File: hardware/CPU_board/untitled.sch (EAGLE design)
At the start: 71 parts, among them IC1 MAX232ECWE, IC2 MAX232ECWE, IC3 AM29F040J, IC4 74HCT138D, IC5 LM2596S, IC6 74245SSOP, IC7 74245SSOP, IC8 74245SSOP, J2 POWER_JACKSLT, U1 AS6C4008-55SIN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

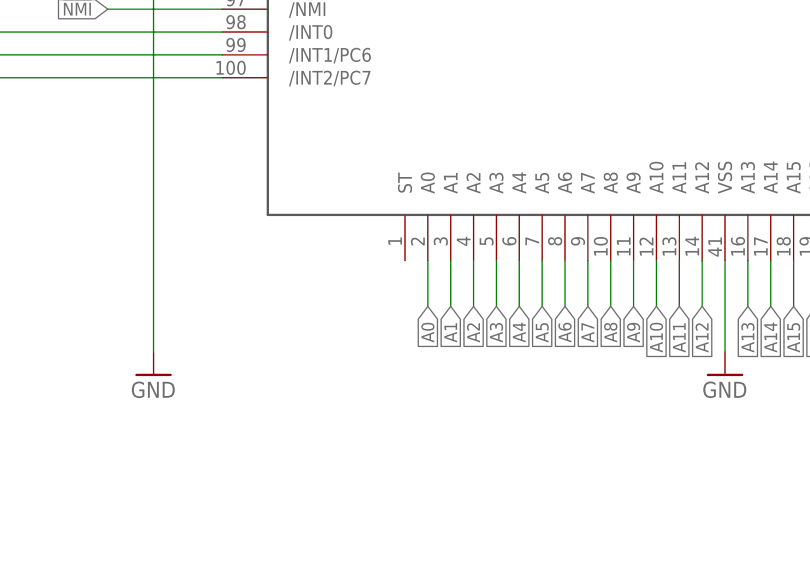
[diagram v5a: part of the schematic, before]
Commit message: ST signal connected (work in progress)
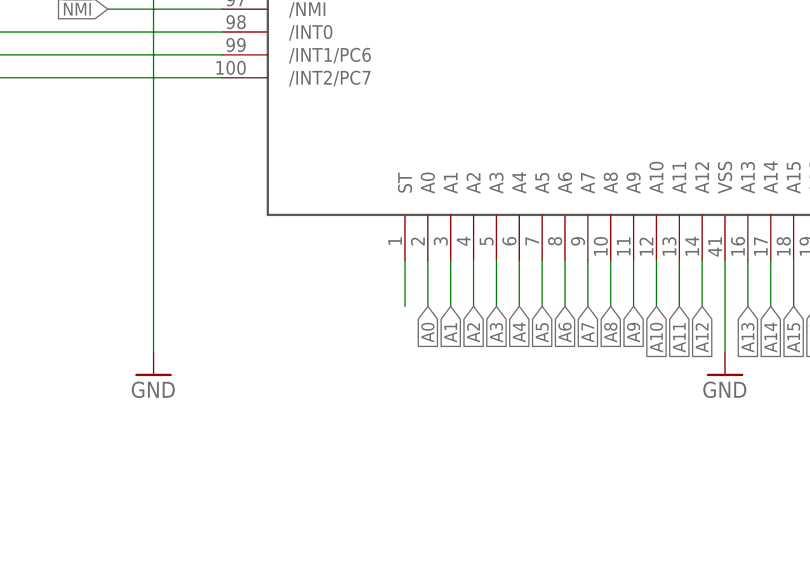
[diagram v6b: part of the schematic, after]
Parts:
- R10: device rcl:R-EU_R0603 -> rcl:R-EU_M1206
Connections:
- new net ST: U$1.ST
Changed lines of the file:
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@@
 <part name="JP5" library="pinhead" deviceset="PINHD-1X2" device=""/>
 <part name="GND16" library="supply1" deviceset="GND" device=""/>
-<part name="R10" library="rcl" deviceset="R-EU_" device="R0603"/>
+<part name="R10" library="rcl" deviceset="R-EU_" device="M1206"/>
 <part name="JP6" library="pinhead" deviceset="PINHD-1X2" device=""/>
 <part name="C21" library="rcl" deviceset="CPOL-EU" device="153CLV-0810" value="220uF"/>
@@
 </segment>
 </net>
+<net name="ST" class="0">
+<segment>
+<pinref part="U$1" gate="G$1" pin="ST"/>
+<wire x1="55.88" y1="35.56" x2="55.88" y2="30.48" width="0.1524" layer="91"/>
+</segment>
+</net>

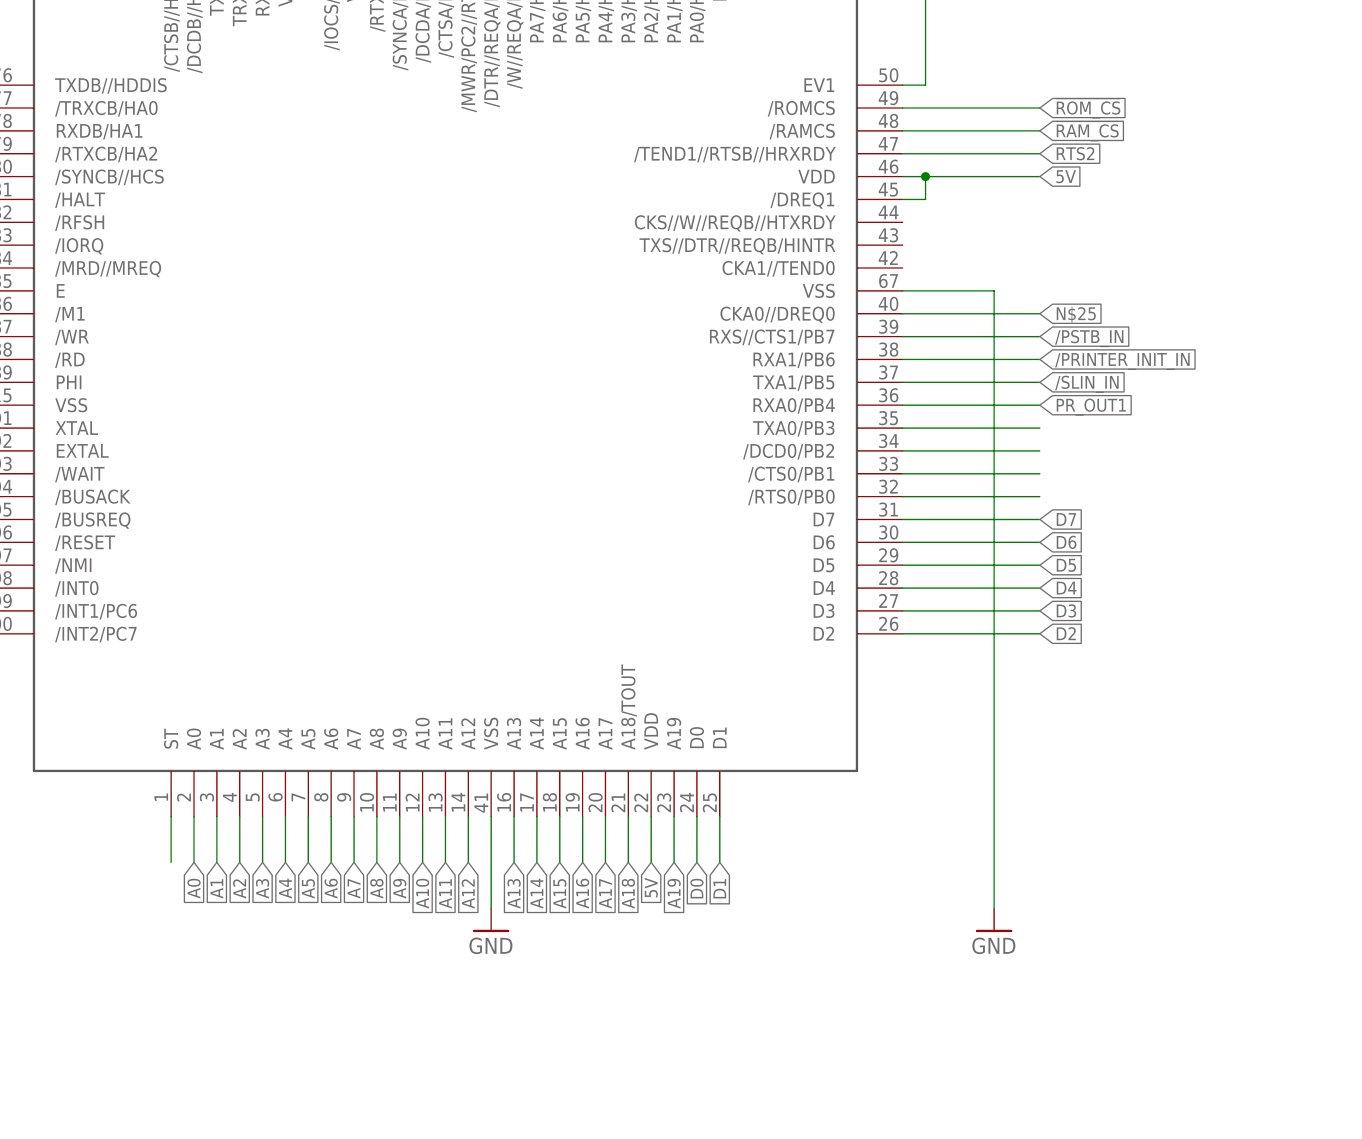
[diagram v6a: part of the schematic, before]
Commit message: Pull-up on ST and DREQ lines added
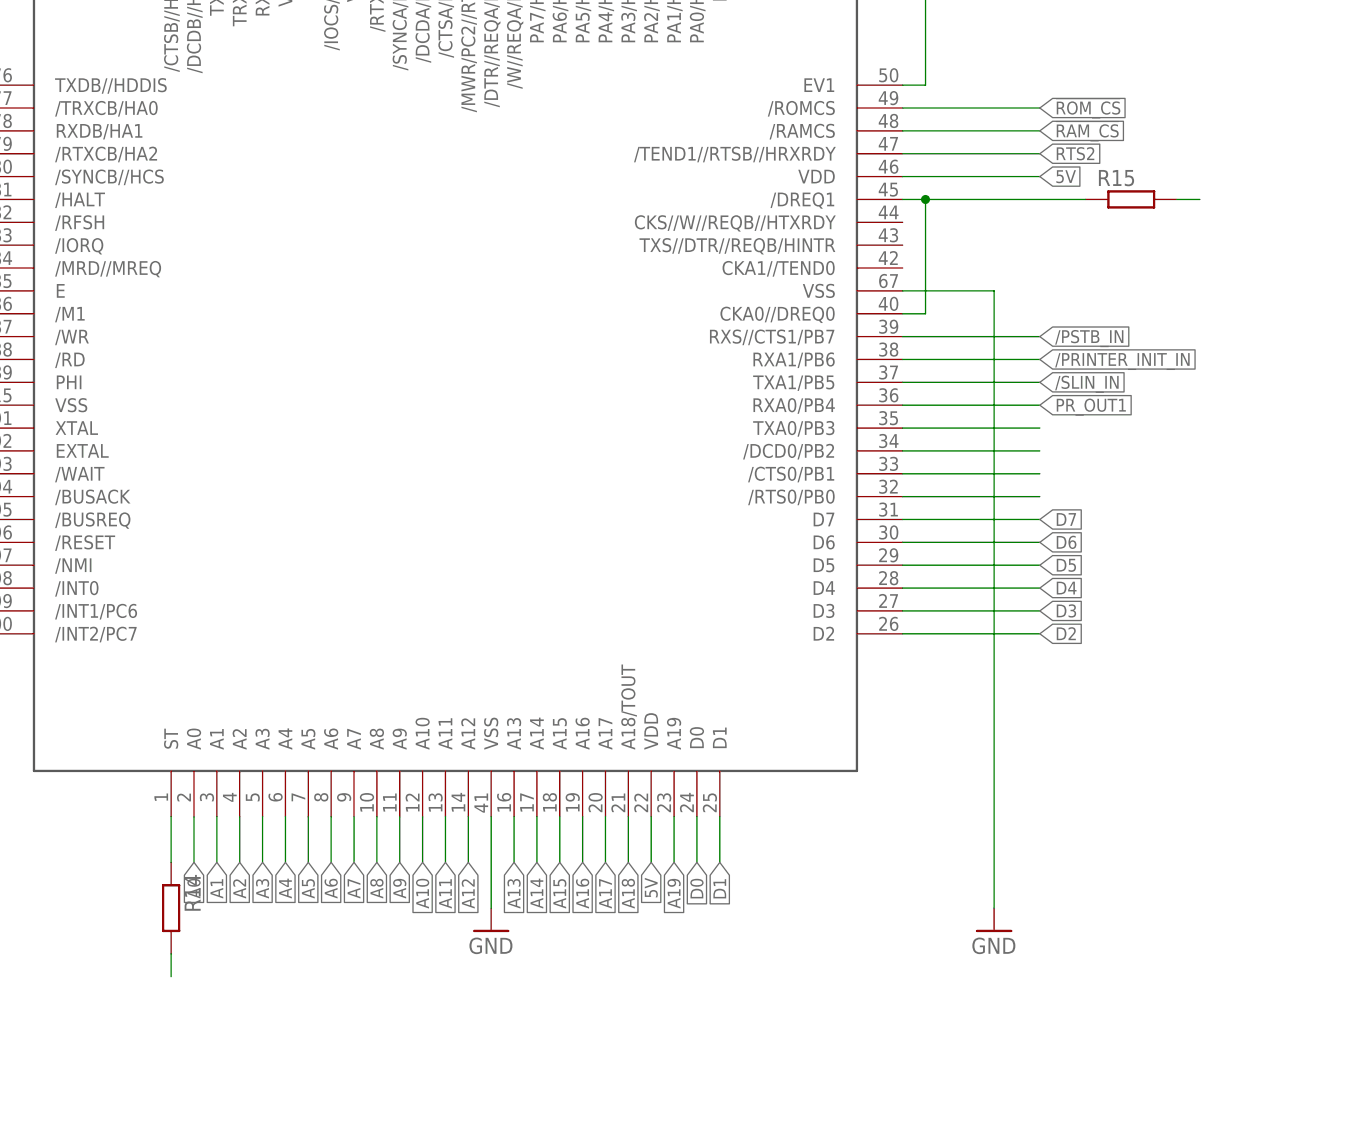
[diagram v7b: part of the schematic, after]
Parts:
- added R14: (no value), rcl:R-EU_0204/5
- added R15: (no value), rcl:R-EU_R0402
- C3: device rcl:C-EUC0603 -> rcl:C-EUC0402
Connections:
- net 5V: now also R14.2, R15.2; no longer U$1./DREQ1
- net N$25: now also R15.1, U$1./DREQ1
- net ST: now also R14.1
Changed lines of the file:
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@@
 <part name="C1" library="rcl" deviceset="C-EU" device="C0603"/>
 <part name="C2" library="rcl" deviceset="C-EU" device="C0603"/>
-<part name="C3" library="rcl" deviceset="C-EU" device="C0603"/>
+<part name="C3" library="rcl" deviceset="C-EU" device="C0402"/>
 <part name="GND5" library="supply1" deviceset="GND" device=""/>
 <part name="X1" library="con-subd" deviceset="M09" device="HP"/>
@@
 <part name="C27" library="rcl" deviceset="C-EU" device="C0402"/>
 <part name="GND26" library="supply1" deviceset="GND" device=""/>
+<part name="R14" library="rcl" deviceset="R-EU_" device="0204/5"/>
+<part name="R15" library="rcl" deviceset="R-EU_" device="R0402"/>
 </parts>
 <sheets>
@@
 <instance part="C27" gate="G$1" x="-43.18" y="190.5"/>
 <instance part="GND26" gate="1" x="147.32" y="132.08"/>
+<instance part="R14" gate="G$1" x="55.88" y="25.4" rot="R270"/>
+<instance part="R15" gate="G$1" x="162.56" y="104.14"/>
 </instances>
 <busses>
@@
 <segment>
 <pinref part="U$1" gate="G$1" pin="VDD@2"/>
-<wire x1="137.16" y1="106.68" x2="139.7" y2="106.68" width="0.1524" layer="91"/>
 <label x="152.4" y="106.68" size="1.4224" layer="95" xref="yes"/>
-<pinref part="U$1" gate="G$1" pin="/DREQ1"/>
-<wire x1="139.7" y1="106.68" x2="152.4" y2="106.68" width="0.1524" layer="91"/>
-<wire x1="137.16" y1="104.14" x2="139.7" y2="104.14" width="0.1524" layer="91"/>
-<wire x1="139.7" y1="104.14" x2="139.7" y2="106.68" width="0.1524" layer="91"/>
-<junction x="139.7" y="106.68"/>
+<wire x1="137.16" y1="106.68" x2="152.4" y2="106.68" width="0.1524" layer="91"/>
 </segment>
 <segment>
@@
 <wire x1="345.44" y1="231.14" x2="345.44" y2="233.68" width="0.1524" layer="91"/>
 </segment>
+<segment>
+<pinref part="R14" gate="G$1" pin="2"/>
+<wire x1="55.88" y1="20.32" x2="55.88" y2="17.78" width="0.1524" layer="91"/>
+</segment>
+<segment>
+<pinref part="R15" gate="G$1" pin="2"/>
+<wire x1="167.64" y1="104.14" x2="170.18" y2="104.14" width="0.1524" layer="91"/>
+</segment>
 </net>
 <net name="TXD1" class="0">
@@
 <segment>
 <pinref part="U$1" gate="G$1" pin="CKA0//DREQ0"/>
-<wire x1="137.16" y1="91.44" x2="152.4" y2="91.44" width="0.1524" layer="91"/>
-<label x="152.4" y="91.44" size="1.4224" layer="95" xref="yes"/>
+<wire x1="137.16" y1="91.44" x2="139.7" y2="91.44" width="0.1524" layer="91"/>
+<pinref part="U$1" gate="G$1" pin="/DREQ1"/>
+<wire x1="137.16" y1="104.14" x2="139.7" y2="104.14" width="0.1524" layer="91"/>
+<wire x1="139.7" y1="91.44" x2="139.7" y2="104.14" width="0.1524" layer="91"/>
+<wire x1="139.7" y1="104.14" x2="157.48" y2="104.14" width="0.1524" layer="91"/>
+<junction x="139.7" y="104.14"/>
+<pinref part="R15" gate="G$1" pin="1"/>
 </segment>
 </net>
@@
 <pinref part="U$1" gate="G$1" pin="ST"/>
 <wire x1="55.88" y1="35.56" x2="55.88" y2="30.48" width="0.1524" layer="91"/>
-</segment>
-</net>
+<pinref part="R14" gate="G$1" pin="1"/>
+</segment>
+</net>

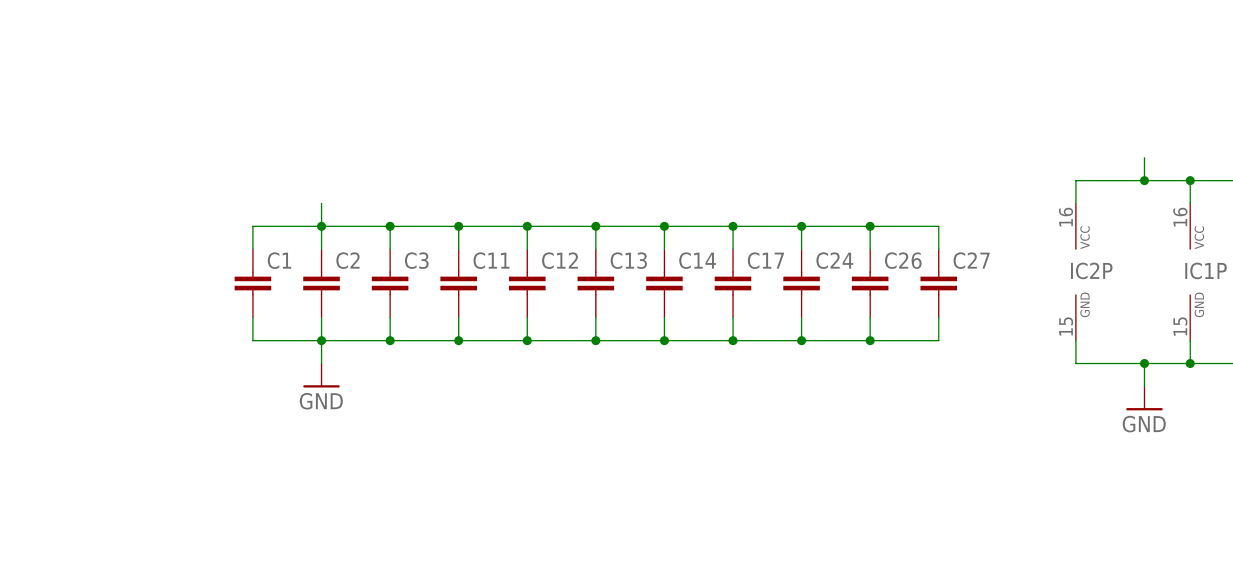
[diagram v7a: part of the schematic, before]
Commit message: Capacitors added
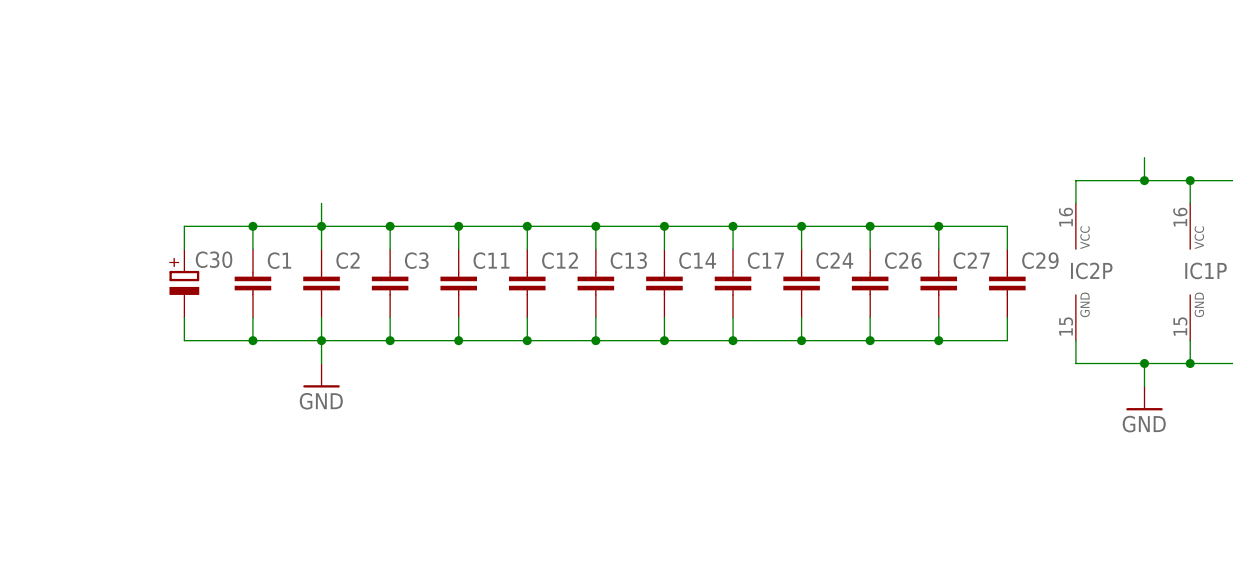
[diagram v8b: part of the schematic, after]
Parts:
- added C29: (no value), rcl:C-EUC0603
- added C30: (no value), rcl:CPOL-EUSMCB
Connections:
- net 5V: now also C29.1, C30.+
- net GND: now also C29.2, C30.-
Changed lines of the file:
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@@
 <part name="R14" library="rcl" deviceset="R-EU_" device="0204/5"/>
 <part name="R15" library="rcl" deviceset="R-EU_" device="R0402"/>
+<part name="C29" library="rcl" deviceset="C-EU" device="C0603"/>
+<part name="C30" library="rcl" deviceset="CPOL-EU" device="SMCB"/>
 </parts>
 <sheets>
@@
 <instance part="R14" gate="G$1" x="55.88" y="25.4" rot="R270"/>
 <instance part="R15" gate="G$1" x="162.56" y="104.14"/>
+<instance part="C29" gate="G$1" x="-35.56" y="190.5"/>
+<instance part="C30" gate="G$1" x="-127" y="190.5"/>
 </instances>
 <busses>
@@
 <wire x1="-43.18" y1="182.88" x2="-43.18" y2="185.42" width="0.1524" layer="91"/>
 <junction x="-50.8" y="182.88"/>
+<pinref part="C29" gate="G$1" pin="2"/>
+<wire x1="-43.18" y1="182.88" x2="-35.56" y2="182.88" width="0.1524" layer="91"/>
+<wire x1="-35.56" y1="182.88" x2="-35.56" y2="185.42" width="0.1524" layer="91"/>
+<junction x="-43.18" y="182.88"/>
+<pinref part="C30" gate="G$1" pin="-"/>
+<wire x1="-119.38" y1="182.88" x2="-127" y2="182.88" width="0.1524" layer="91"/>
+<wire x1="-127" y1="182.88" x2="-127" y2="185.42" width="0.1524" layer="91"/>
+<junction x="-119.38" y="182.88"/>
 </segment>
 <segment>
@@
 <wire x1="-43.18" y1="195.58" x2="-43.18" y2="193.04" width="0.1524" layer="91"/>
 <junction x="-50.8" y="195.58"/>
-</segment>
-<segment>
+<pinref part="C29" gate="G$1" pin="1"/>
+<wire x1="-43.18" y1="195.58" x2="-35.56" y2="195.58" width="0.1524" layer="91"/>
+<wire x1="-35.56" y1="195.58" x2="-35.56" y2="193.04" width="0.1524" layer="91"/>
+<junction x="-43.18" y="195.58"/>
+<pinref part="C30" gate="G$1" pin="+"/>
+<wire x1="-119.38" y1="195.58" x2="-127" y2="195.58" width="0.1524" layer="91"/>
+<wire x1="-127" y1="195.58" x2="-127" y2="193.04" width="0.1524" layer="91"/>
+<junction x="-119.38" y="195.58"/>
+</segment>
+<segment>
